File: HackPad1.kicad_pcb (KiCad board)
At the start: 2 copper layers, 0 parts

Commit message: pcb basics
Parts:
- added BT1: 3.3V Cell, Battery:BatteryHolder_Keystone_104_1x23mm, F.Cu at (108.7, 77.5)
- added D1: LED, LED_THT:LED_D3.0mm_Horizontal_O1.27mm_Z2.0mm_IRGrey, F.Cu at (146.7, 85.8)
- added MK1: Microphone_Condenser, Buzzer_Beeper:Buzzer_D14mm_H7mm_P10mm, F.Cu at (144.5, 96.8)
- added R1: R, Resistor_THT:R_Axial_DIN0309_L9.0mm_D3.2mm_P12.70mm_Horizontal, F.Cu at (141.0, 69.0)
- added R2: LDR07, OptoDevice:R_LDR_5.1x4.3mm_P3.4mm_Vertical, F.Cu at (159.0, 86.2)
- added R3: R, Resistor_THT:R_Axial_DIN0309_L9.0mm_D3.2mm_P12.70mm_Horizontal, F.Cu at (141.0, 73.8)
- added R4: R, Resistor_THT:R_Axial_DIN0309_L9.0mm_D3.2mm_P12.70mm_Horizontal, F.Cu at (141.0, 78.5)
- added SW1: SW_SPDT, Button_Switch_SMD:Nidec_Copal_CAS-120A, F.Cu at (134.7, 101.1)
- added U1: ATtiny85V-10P, Package_DIP:DIP-8_W7.62mm, F.Cu at (118.5, 94.9)
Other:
- board outline added: 60 x 60 mm

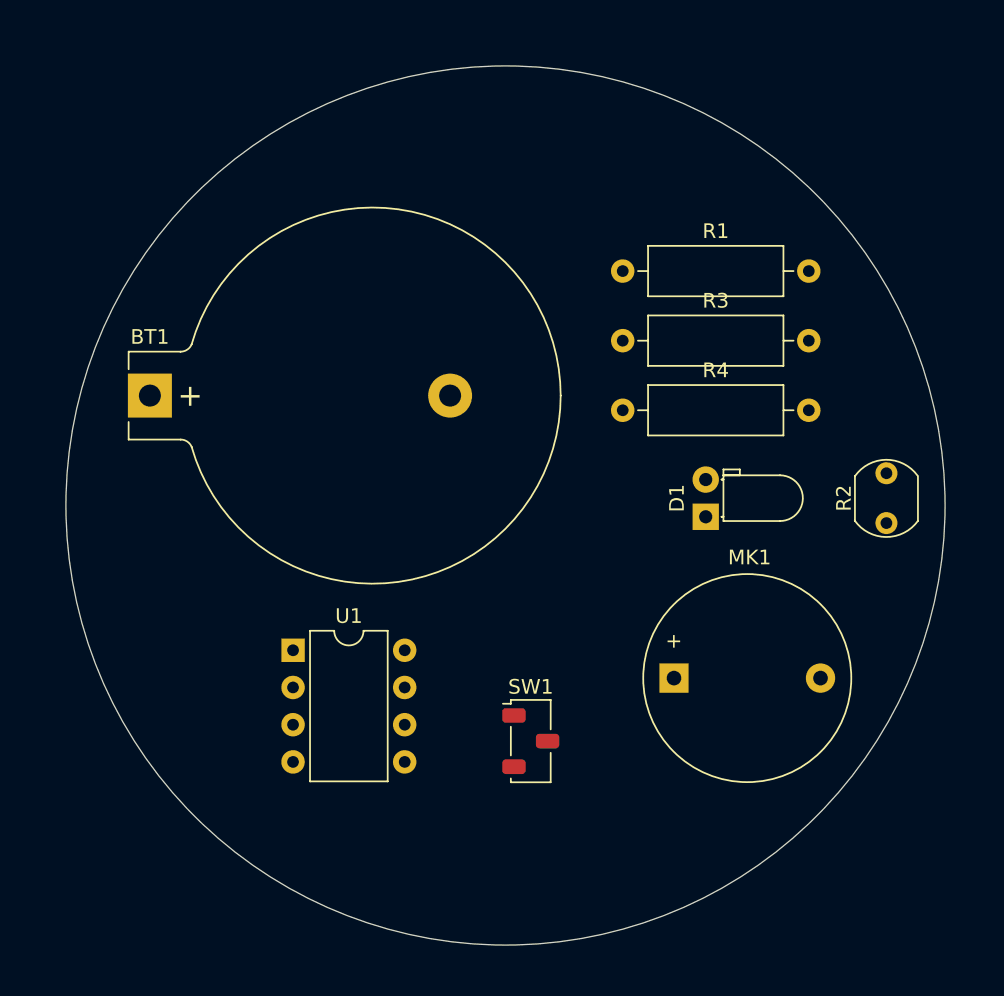
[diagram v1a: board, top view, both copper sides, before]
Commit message: changed layout
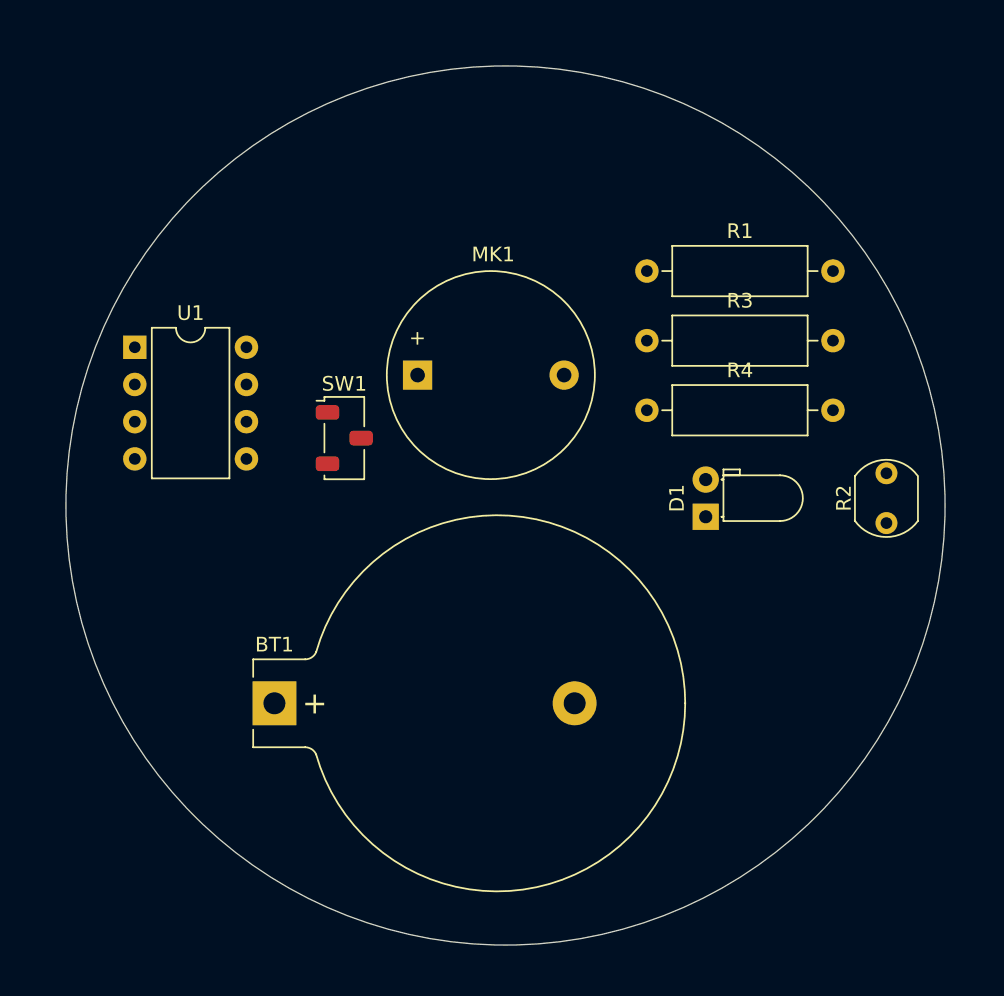
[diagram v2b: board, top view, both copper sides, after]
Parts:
- moved MK1 27.1 mm to (127.0, 76.1)
- moved SW1 24.3 mm to (122.0, 80.4)
- moved U1 23.3 mm to (107.7, 74.2)
- moved BT1 22.7 mm to (117.2, 98.5)
- moved R1 1.65 mm to (142.7, 69.0)
- moved R3 1.65 mm to (142.7, 73.8)
- moved R4 1.65 mm to (142.7, 78.5)
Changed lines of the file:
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@@
 	(footprint "Resistor_THT:R_Axial_DIN0309_L9.0mm_D3.2mm_P12.70mm_Horizontal"
 		(layer "F.Cu")
-		(at 141 69)
+		(at 142.65 69)
 		(descr "Resistor, Axial_DIN0309 series, Axial, Horizontal, pin pitch=12.7mm, 0.5W = 1/2W, length*diameter=9*3.2mm^2, http://cdn-reichelt.de/documents/datenblatt/B400/1_4W%23YAG.pdf")
 		(tags "Resistor Axial_DIN0309 series Axial Horizontal pin pitch 12.7mm 0.5W = 1/2W length 9mm diameter 3.2mm")
@@
 	(footprint "Package_DIP:DIP-8_W7.62mm"
 		(layer "F.Cu")
-		(at 118.5 94.88)
+		(at 107.7 74.2)
 		(descr "8-lead though-hole mounted DIP package, row spacing 7.62 mm (300 mils)")
 		(tags "THT DIP DIL PDIP 2.54mm 7.62mm 300mil")
@@
 	(footprint "Resistor_THT:R_Axial_DIN0309_L9.0mm_D3.2mm_P12.70mm_Horizontal"
 		(layer "F.Cu")
-		(at 141 73.75)
+		(at 142.65 73.75)
 		(descr "Resistor, Axial_DIN0309 series, Axial, Horizontal, pin pitch=12.7mm, 0.5W = 1/2W, length*diameter=9*3.2mm^2, http://cdn-reichelt.de/documents/datenblatt/B400/1_4W%23YAG.pdf")
 		(tags "Resistor Axial_DIN0309 series Axial Horizontal pin pitch 12.7mm 0.5W = 1/2W length 9mm diameter 3.2mm")
@@
 	(footprint "Buzzer_Beeper:Buzzer_D14mm_H7mm_P10mm"
 		(layer "F.Cu")
-		(at 144.5 96.78)
+		(at 127 76.1)
 		(descr "Generic Buzzer, D14mm height 7mm with pitch 10mm")
 		(tags "buzzer")
@@
 	(footprint "Battery:BatteryHolder_Keystone_104_1x23mm"
 		(layer "F.Cu")
-		(at 108.73 77.5)
+		(at 117.23 98.5)
 		(descr "http://www.keyelco.com/product-pdf.cfm?p=744")
 		(tags "Keystone type 104 battery holder")
@@
 	(footprint "Button_Switch_SMD:Nidec_Copal_CAS-120A"
 		(layer "F.Cu")
-		(at 134.725 101.08)
+		(at 122 80.4)
 		(descr "Slide Switch, SMD, Nidec CAS series, https://www.nidec-components.com/e/catalog/switch/cas.pdf")
 		(tags "SMD slide switch Nidec CAS 120A ")
@@
 	(footprint "Resistor_THT:R_Axial_DIN0309_L9.0mm_D3.2mm_P12.70mm_Horizontal"
 		(layer "F.Cu")
-		(at 141 78.5)
+		(at 142.65 78.5)
 		(descr "Resistor, Axial_DIN0309 series, Axial, Horizontal, pin pitch=12.7mm, 0.5W = 1/2W, length*diameter=9*3.2mm^2, http://cdn-reichelt.de/documents/datenblatt/B400/1_4W%23YAG.pdf")
 		(tags "Resistor Axial_DIN0309 series Axial Horizontal pin pitch 12.7mm 0.5W = 1/2W length 9mm diameter 3.2mm")

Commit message: designed pcb routing basics
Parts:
- moved U1 27.1 mm to (131.2, 60.7)
- moved R3 14.5 mm to (130.2, 81.0)
- moved R4 13.0 mm to (130.2, 75.0)
- moved MK1 10.5 mm to (116.5, 75.5)
- moved SW1 10.5 mm to (111.5, 80.4)
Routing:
- net GND: track 0.00 -> 103.4 mm
- net +3.3V: track 0.00 -> 75.3 mm
- net Net-(BT1--): track 0.00 -> 36.0 mm
- net /MIC: track 0.00 -> 32.8 mm
- net /LDR: track 0.00 -> 31.3 mm
- net Net-(D1-K): track 0.00 -> 24.9 mm
- added copper zone on F.Cu, net GND
